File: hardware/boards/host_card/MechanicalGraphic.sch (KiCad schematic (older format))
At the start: 7 parts

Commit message: More fiddling with the DM stuff
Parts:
- added H?: MountingHole_Pad, MountingHole:MountingHole_3.2mm_M3_Pad_Via, symbol Mechanical:MountingHole_Pad
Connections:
- new net GND: H?.1
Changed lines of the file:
@@
 	1    0    0    -1
 $EndComp
+$Comp
+L Mechanical:MountingHole_Pad H?
+U 1 1 5EEC9E4D
+P 1650 3750
+F 0 "H?" H 1750 3799 50  0000 L CNN
+F 1 "MountingHole_Pad" H 1750 3708 50  0000 L CNN
+F 2 "MountingHole:MountingHole_3.2mm_M3_Pad_Via" H 1650 3750 50  0001 C CNN
+F 3 "~" H 1650 3750 50  0001 C CNN
+	1    1650 3750
+	1    0    0    -1
+$EndComp
+$Comp
+L power:GND #PWR?
+U 1 1 5EECB465
+P 1650 4200
+F 0 "#PWR?" H 1650 3950 50  0001 C CNN
+F 1 "GND" H 1655 4027 50  0000 C CNN
+F 2 "" H 1650 4200 50  0001 C CNN
+F 3 "" H 1650 4200 50  0001 C CNN
+	1    1650 4200
+	1    0    0    -1
+$EndComp
+Wire Wire Line
+	1650 3850 1650 4200
 $EndSCHEMATC

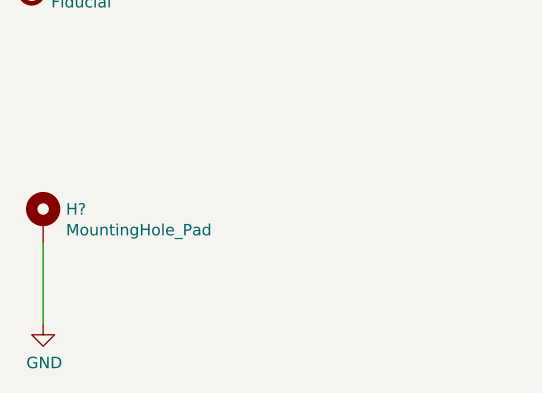
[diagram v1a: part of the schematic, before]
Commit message: Updated the generic SODIMM part footprint to use the new Debug Module footprint
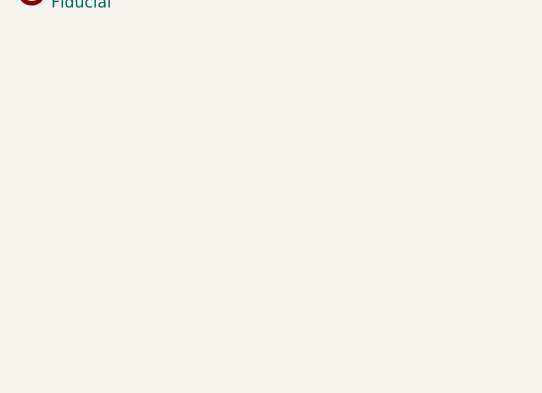
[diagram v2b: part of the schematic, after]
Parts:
- removed H?: MountingHole_Pad, MountingHole:MountingHole_3.2mm_M3_Pad_Via, symbol Mechanical:MountingHole_Pad
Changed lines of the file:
@@
 	1    0    0    -1
 $EndComp
-$Comp
-L Mechanical:MountingHole_Pad H?
-U 1 1 5EEC9E4D
-P 1650 3750
-F 0 "H?" H 1750 3799 50  0000 L CNN
-F 1 "MountingHole_Pad" H 1750 3708 50  0000 L CNN
-F 2 "MountingHole:MountingHole_3.2mm_M3_Pad_Via" H 1650 3750 50  0001 C CNN
-F 3 "~" H 1650 3750 50  0001 C CNN
-	1    1650 3750
-	1    0    0    -1
-$EndComp
-$Comp
-L power:GND #PWR?
-U 1 1 5EECB465
-P 1650 4200
-F 0 "#PWR?" H 1650 3950 50  0001 C CNN
-F 1 "GND" H 1655 4027 50  0000 C CNN
-F 2 "" H 1650 4200 50  0001 C CNN
-F 3 "" H 1650 4200 50  0001 C CNN
-	1    1650 4200
-	1    0    0    -1
-$EndComp
-Wire Wire Line
-	1650 3850 1650 4200
 $EndSCHEMATC
